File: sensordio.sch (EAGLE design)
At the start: 15 parts

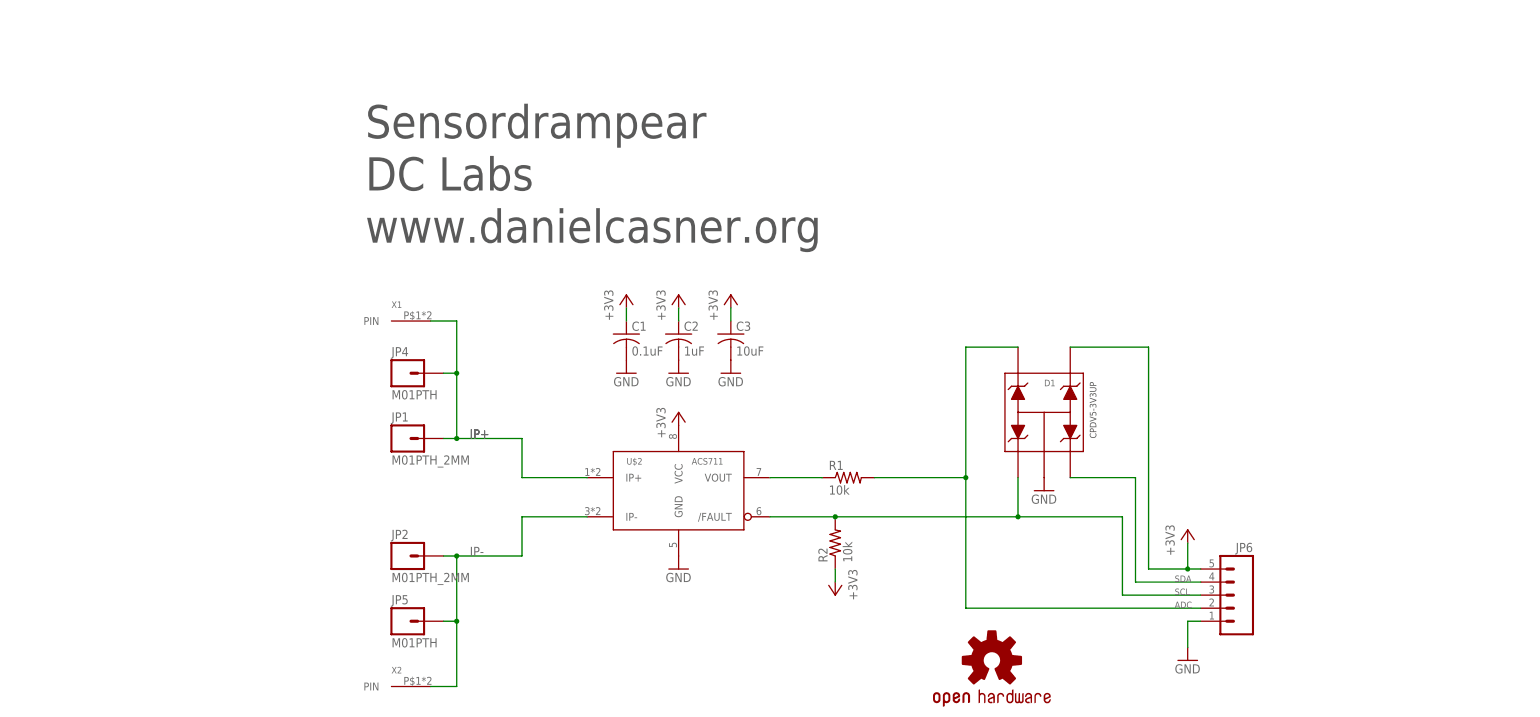
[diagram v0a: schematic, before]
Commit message: Add GPIO extension for sensordrone.
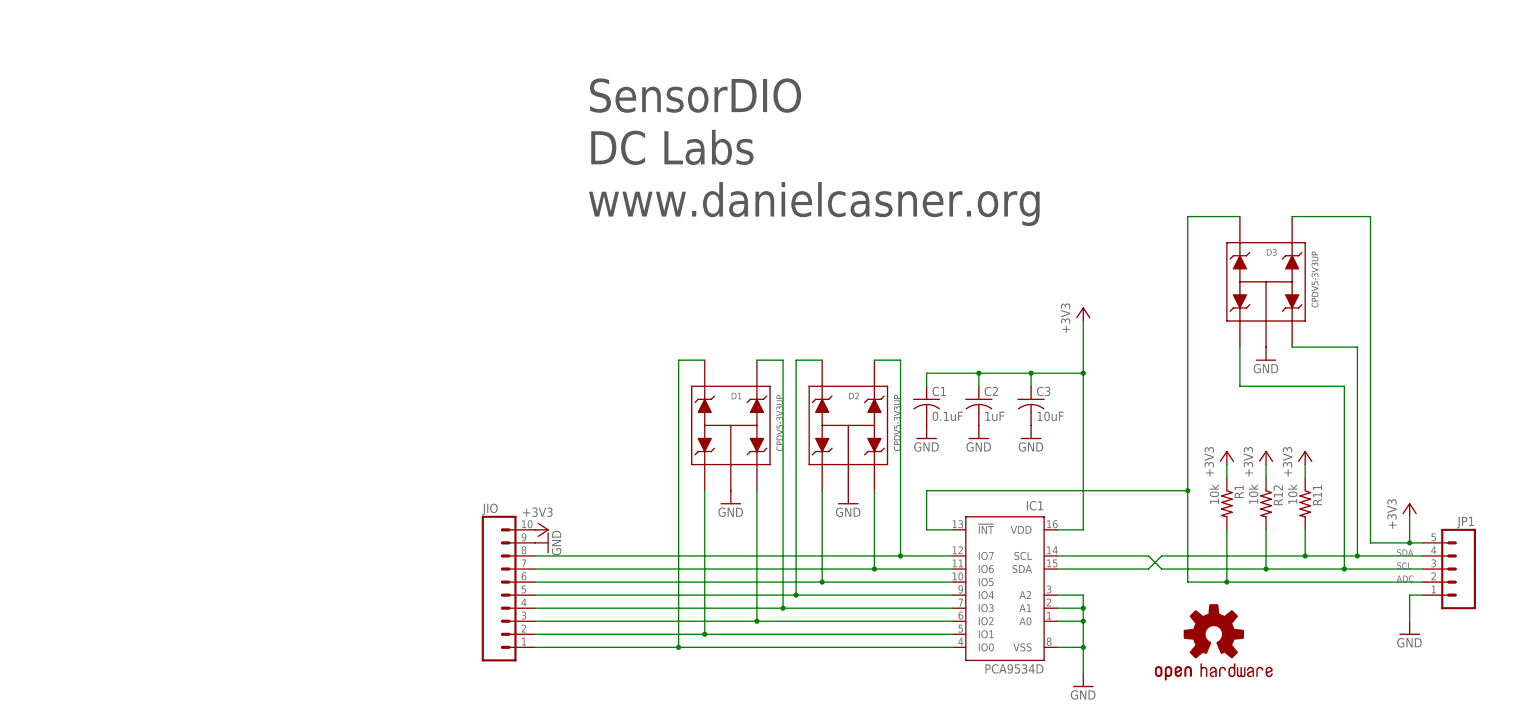
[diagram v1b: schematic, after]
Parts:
- removed JP2: M01PTH_2MM, SparkFun:M01PTH_2MM
- removed JP4, JP5: M01PTH, SparkFun:M01PTH
- removed JP6: (no value), SparkFun-Connectors:M05PTH_LONGPADS
- removed R2: 10k, rcl:R-US_R0402
- removed U$2: ACS711, DMM:ACS711
- removed X1, X2: (no value), DMM:606X
- added D2, D3: CPDV5-3V3UP, DMM:CPDV5
- added IC1: PCA9534D, micro-philips:PCA9534D
- added JIO: (no value), con-amp-quick:M10
- added R11, R12: 10k, rcl:R-US_R0402
- JP1: value M01PTH_2MM -> (none); device SparkFun:M01PTH_2MM -> SparkFun-Connectors:M05PTH_LONGPADS
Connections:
- removed net IP+: JP1.1, JP4.1, U$2.IP+, X1.PIN
- removed net IP-: JP2.1, JP5.1, U$2.IP-, X2.PIN
- new net N$2: D1.P$5, IC1.IO0, JIO.1
- new net N$4: D1.P$3, IC1.IO2, JIO.3
- new net N$5: D1.P$4, IC1.IO3, JIO.4
- new net N$6: D2.P$5, IC1.IO4, JIO.5
- new net N$7: D2.P$1, IC1.IO5, JIO.6
- new net N$8: D2.P$3, IC1.IO6, JIO.7
- new net N$9: D2.P$4, IC1.IO7, JIO.8
- net +3V3: now also D3.P$4, IC1.VDD, JIO.10, JP1.5, R1.1, R11.1, R12.1; no longer D1.P$4, JP6.5, R2.1, U$2.VCC
- net ADC: now also D3.P$5, IC1.!INT, JP1.2; no longer D1.P$5, JP6.2
- net GND: now also D2.P$2, D3.P$2, IC1.A0, IC1.A1, IC1.A2, IC1.VSS, JIO.9, JP1.1; no longer JP6.1, U$2.GND
- net N$3: now also D1.P$1, IC1.IO1, JIO.2; no longer R1.1, U$2.VOUT
- net SCL: now also D3.P$1, IC1.SCL, JP1.3, R12.2; no longer D1.P$1, JP6.3, R2.2, U$2./FAULT
- net SDA: now also D3.P$3, IC1.SDA, JP1.4, R11.2; no longer D1.P$3, JP6.4
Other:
- note added: "SensorDIO"
- note removed: "Sensordrampear"
- moved on the sheet: C1, C2, C3, D1, R1

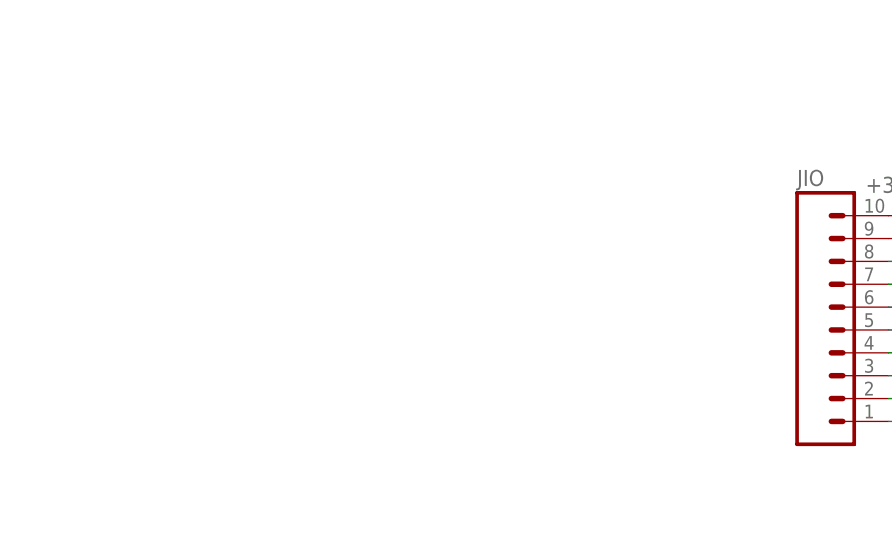
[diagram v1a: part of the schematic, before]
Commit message: Add add-on add-on for SensordrIO
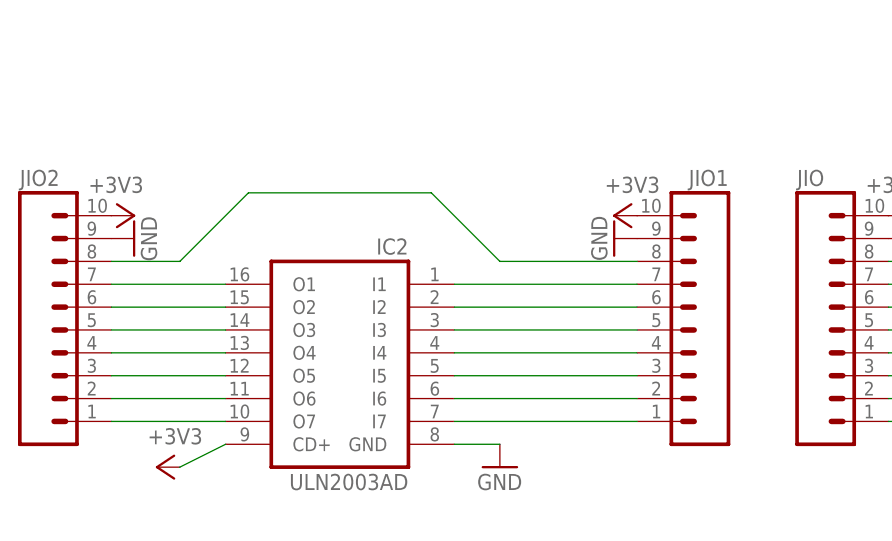
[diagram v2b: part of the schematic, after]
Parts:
- added IC2: ULN2003AD, uln-udn:ULN2003AD
- added JIO1, JIO2: (no value), con-amp-quick:M10
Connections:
- new net N$1: IC2.I7, JIO1.1
- new net N$10: IC2.I6, JIO1.2
- new net N$11: IC2.I5, JIO1.3
- new net N$12: IC2.I4, JIO1.4
- new net N$13: IC2.I3, JIO1.5
- new net N$14: IC2.I2, JIO1.6
- new net N$15: IC2.I1, JIO1.7
- new net N$16: IC2.O7, JIO2.1
- new net N$17: IC2.O6, JIO2.2
- new net N$18: IC2.O5, JIO2.3
- new net N$19: IC2.O4, JIO2.4
- new net N$20: IC2.O3, JIO2.5
- new net N$21: IC2.O2, JIO2.6
- new net N$22: IC2.O1, JIO2.7
- new net N$23: JIO1.8, JIO2.8
- net +3V3: now also IC2.CD+, JIO1.10, JIO2.10
- net GND: now also IC2.GND, JIO1.9, JIO2.9
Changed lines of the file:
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@@
 <part name="GND8" library="supply1" deviceset="GND" device=""/>
 <part name="+3V6" library="supply1" deviceset="+3V3" device=""/>
+<part name="IC2" library="uln-udn" deviceset="ULN2003A" device="D"/>
+<part name="JIO1" library="con-amp-quick" deviceset="M10" device=""/>
+<part name="JIO2" library="con-amp-quick" deviceset="M10" device=""/>
+<part name="GND9" library="supply1" deviceset="GND" device=""/>
+<part name="GND10" library="supply1" deviceset="GND" device=""/>
+<part name="GND12" library="supply1" deviceset="GND" device=""/>
+<part name="+3V7" library="supply1" deviceset="+3V3" device=""/>
+<part name="+3V8" library="supply1" deviceset="+3V3" device=""/>
+<part name="+3V9" library="supply1" deviceset="+3V3" device=""/>
 </parts>
 <sheets>
@@
 <instance part="GND8" gate="1" x="-86.36" y="22.86" rot="R90"/>
 <instance part="+3V6" gate="G$1" x="-86.36" y="25.4" rot="R270"/>
+<instance part="IC2" gate="A" x="-149.86" y="10.16" rot="MR0"/>
+<instance part="JIO1" gate="G$1" x="-111.76" y="15.24" rot="MR0"/>
+<instance part="JIO2" gate="G$1" x="-180.34" y="15.24"/>
+<instance part="GND9" gate="1" x="-132.08" y="-2.54"/>
+<instance part="GND10" gate="1" x="-119.38" y="22.86" rot="R270"/>
+<instance part="GND12" gate="1" x="-172.72" y="22.86" rot="R90"/>
+<instance part="+3V7" gate="G$1" x="-172.72" y="25.4" rot="R270"/>
+<instance part="+3V8" gate="G$1" x="-119.38" y="25.4" rot="MR270"/>
+<instance part="+3V9" gate="G$1" x="-170.18" y="-2.54" rot="MR270"/>
 </instances>
 <busses>
@@
 <pinref part="JIO" gate="G$1" pin="9"/>
 <pinref part="GND8" gate="1" pin="GND"/>
+</segment>
+<segment>
+<pinref part="IC2" gate="A" pin="GND"/>
+<pinref part="GND9" gate="1" pin="GND"/>
+<wire x1="-132.08" y1="0" x2="-137.16" y2="0" width="0.1524" layer="91"/>
+</segment>
+<segment>
+<pinref part="JIO1" gate="G$1" pin="9"/>
+<pinref part="GND10" gate="1" pin="GND"/>
+</segment>
+<segment>
+<pinref part="JIO2" gate="G$1" pin="9"/>
+<pinref part="GND12" gate="1" pin="GND"/>
 </segment>
 </net>
@@
 <pinref part="+3V6" gate="G$1" pin="+3V3"/>
 </segment>
+<segment>
+<pinref part="JIO2" gate="G$1" pin="10"/>
+<pinref part="+3V7" gate="G$1" pin="+3V3"/>
+</segment>
+<segment>
+<pinref part="JIO1" gate="G$1" pin="10"/>
+<pinref part="+3V8" gate="G$1" pin="+3V3"/>
+</segment>
+<segment>
+<pinref part="IC2" gate="A" pin="CD+"/>
+<pinref part="+3V9" gate="G$1" pin="+3V3"/>
+<wire x1="-167.64" y1="-2.54" x2="-162.56" y2="0" width="0.1524" layer="91"/>
+</segment>
 </net>
 <net name="SDA" class="0">
@@
 </segment>
 </net>
+<net name="N$1" class="0">
+<segment>
+<pinref part="JIO1" gate="G$1" pin="1"/>
+<pinref part="IC2" gate="A" pin="I7"/>
+<wire x1="-116.84" y1="2.54" x2="-137.16" y2="2.54" width="0.1524" layer="91"/>
+</segment>
+</net>
+<net name="N$10" class="0">
+<segment>
+<pinref part="JIO1" gate="G$1" pin="2"/>
+<pinref part="IC2" gate="A" pin="I6"/>
+<wire x1="-116.84" y1="5.08" x2="-137.16" y2="5.08" width="0.1524" layer="91"/>
+</segment>
+</net>
+<net name="N$11" class="0">
+<segment>
+<pinref part="JIO1" gate="G$1" pin="3"/>
+<pinref part="IC2" gate="A" pin="I5"/>
+<wire x1="-116.84" y1="7.62" x2="-137.16" y2="7.62" width="0.1524" layer="91"/>
+</segment>
+</net>
+<net name="N$12" class="0">
+<segment>
+<pinref part="JIO1" gate="G$1" pin="4"/>
+<pinref part="IC2" gate="A" pin="I4"/>
+<wire x1="-116.84" y1="10.16" x2="-137.16" y2="10.16" width="0.1524" layer="91"/>
+</segment>
+</net>
+<net name="N$13" class="0">
+<segment>
+<pinref part="JIO1" gate="G$1" pin="5"/>
+<pinref part="IC2" gate="A" pin="I3"/>
+<wire x1="-116.84" y1="12.7" x2="-137.16" y2="12.7" width="0.1524" layer="91"/>
+</segment>
+</net>
+<net name="N$14" class="0">
+<segment>
+<pinref part="JIO1" gate="G$1" pin="6"/>
+<pinref part="IC2" gate="A" pin="I2"/>
+<wire x1="-116.84" y1="15.24" x2="-137.16" y2="15.24" width="0.1524" layer="91"/>
+</segment>
+</net>
+<net name="N$15" class="0">
+<segment>
+<pinref part="JIO1" gate="G$1" pin="7"/>
+<pinref part="IC2" gate="A" pin="I1"/>
+<wire x1="-116.84" y1="17.78" x2="-137.16" y2="17.78" width="0.1524" layer="91"/>
+</segment>
+</net>
+<net name="N$16" class="0">
+<segment>
+<pinref part="JIO2" gate="G$1" pin="1"/>
+<pinref part="IC2" gate="A" pin="O7"/>
+<wire x1="-175.26" y1="2.54" x2="-162.56" y2="2.54" width="0.1524" layer="91"/>
+</segment>
+</net>
+<net name="N$17" class="0">
+<segment>
+<pinref part="JIO2" gate="G$1" pin="2"/>
+<pinref part="IC2" gate="A" pin="O6"/>
+<wire x1="-175.26" y1="5.08" x2="-162.56" y2="5.08" width="0.1524" layer="91"/>
+</segment>
+</net>
+<net name="N$18" class="0">
+<segment>
+<pinref part="JIO2" gate="G$1" pin="3"/>
+<pinref part="IC2" gate="A" pin="O5"/>
+<wire x1="-175.26" y1="7.62" x2="-162.56" y2="7.62" width="0.1524" layer="91"/>
+</segment>
+</net>
+<net name="N$19" class="0">
+<segment>
+<pinref part="JIO2" gate="G$1" pin="4"/>
+<pinref part="IC2" gate="A" pin="O4"/>
+<wire x1="-175.26" y1="10.16" x2="-162.56" y2="10.16" width="0.1524" layer="91"/>
+</segment>
+</net>
+<net name="N$20" class="0">
+<segment>
+<pinref part="JIO2" gate="G$1" pin="5"/>
+<pinref part="IC2" gate="A" pin="O3"/>
+<wire x1="-175.26" y1="12.7" x2="-162.56" y2="12.7" width="0.1524" layer="91"/>
+</segment>
+</net>
+<net name="N$21" class="0">
+<segment>
+<pinref part="JIO2" gate="G$1" pin="6"/>
+<pinref part="IC2" gate="A" pin="O2"/>
+<wire x1="-175.26" y1="15.24" x2="-162.56" y2="15.24" width="0.1524" layer="91"/>
+</segment>
+</net>
+<net name="N$22" class="0">
+<segment>
+<pinref part="JIO2" gate="G$1" pin="7"/>
+<pinref part="IC2" gate="A" pin="O1"/>
+<wire x1="-175.26" y1="17.78" x2="-162.56" y2="17.78" width="0.1524" layer="91"/>
+</segment>
+</net>
+<net name="N$23" class="0">
+<segment>
+<pinref part="JIO2" gate="G$1" pin="8"/>
+<wire x1="-175.26" y1="20.32" x2="-167.64" y2="20.32" width="0.1524" layer="91"/>
+<wire x1="-167.64" y1="20.32" x2="-160.02" y2="27.94" width="0.1524" layer="91"/>
+<wire x1="-160.02" y1="27.94" x2="-139.7" y2="27.94" width="0.1524" layer="91"/>
+<wire x1="-139.7" y1="27.94" x2="-132.08" y2="20.32" width="0.1524" layer="91"/>
+<pinref part="JIO1" gate="G$1" pin="8"/>
+<wire x1="-132.08" y1="20.32" x2="-116.84" y2="20.32" width="0.1524" layer="91"/>
+</segment>
+</net>

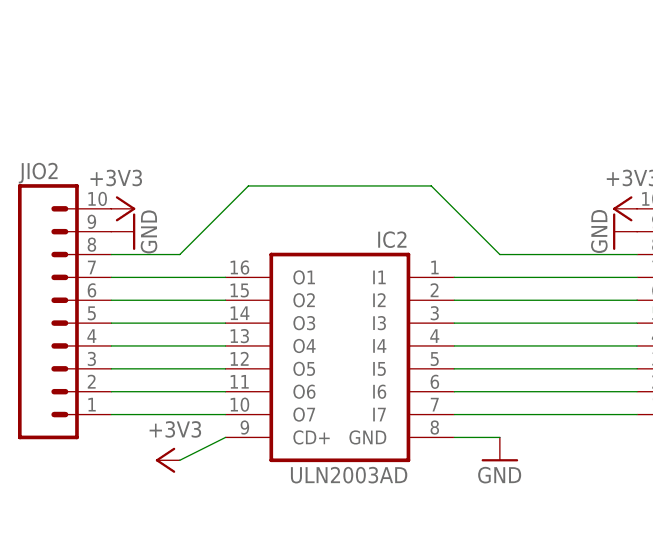
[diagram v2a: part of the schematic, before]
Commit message: Add pin signal labels
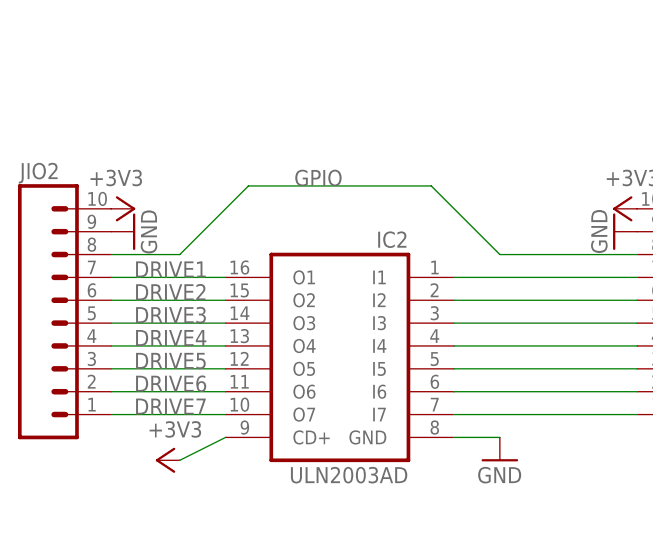
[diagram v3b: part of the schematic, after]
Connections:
- net N$16 renamed DRIVE7
- net N$17 renamed DRIVE6
- net N$18 renamed DRIVE5
- net N$19 renamed DRIVE4
- net N$20 renamed DRIVE3
- net N$21 renamed DRIVE2
- net N$22 renamed DRIVE1
- net N$23 renamed GPIO
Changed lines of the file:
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@@
 </segment>
 </net>
-<net name="N$16" class="0">
+<net name="DRIVE7" class="0">
 <segment>
 <pinref part="JIO2" gate="G$1" pin="1"/>
 <pinref part="IC2" gate="A" pin="O7"/>
 <wire x1="-175.26" y1="2.54" x2="-162.56" y2="2.54" width="0.1524" layer="91"/>
+<label x="-172.72" y="2.54" size="1.778" layer="95"/>
 </segment>
 </net>
-<net name="N$17" class="0">
+<net name="DRIVE6" class="0">
 <segment>
 <pinref part="JIO2" gate="G$1" pin="2"/>
 <pinref part="IC2" gate="A" pin="O6"/>
 <wire x1="-175.26" y1="5.08" x2="-162.56" y2="5.08" width="0.1524" layer="91"/>
+<label x="-172.72" y="5.08" size="1.778" layer="95"/>
 </segment>
 </net>
-<net name="N$18" class="0">
+<net name="DRIVE5" class="0">
 <segment>
 <pinref part="JIO2" gate="G$1" pin="3"/>
 <pinref part="IC2" gate="A" pin="O5"/>
 <wire x1="-175.26" y1="7.62" x2="-162.56" y2="7.62" width="0.1524" layer="91"/>
+<label x="-172.72" y="7.62" size="1.778" layer="95"/>
 </segment>
 </net>
-<net name="N$19" class="0">
+<net name="DRIVE4" class="0">
 <segment>
 <pinref part="JIO2" gate="G$1" pin="4"/>
 <pinref part="IC2" gate="A" pin="O4"/>
 <wire x1="-175.26" y1="10.16" x2="-162.56" y2="10.16" width="0.1524" layer="91"/>
+<label x="-172.72" y="10.16" size="1.778" layer="95"/>
 </segment>
 </net>
-<net name="N$20" class="0">
+<net name="DRIVE3" class="0">
 <segment>
 <pinref part="JIO2" gate="G$1" pin="5"/>
 <pinref part="IC2" gate="A" pin="O3"/>
 <wire x1="-175.26" y1="12.7" x2="-162.56" y2="12.7" width="0.1524" layer="91"/>
+<label x="-172.72" y="12.7" size="1.778" layer="95"/>
 </segment>
 </net>
-<net name="N$21" class="0">
+<net name="DRIVE2" class="0">
 <segment>
 <pinref part="JIO2" gate="G$1" pin="6"/>
 <pinref part="IC2" gate="A" pin="O2"/>
 <wire x1="-175.26" y1="15.24" x2="-162.56" y2="15.24" width="0.1524" layer="91"/>
+<label x="-172.72" y="15.24" size="1.778" layer="95"/>
 </segment>
 </net>
-<net name="N$22" class="0">
+<net name="DRIVE1" class="0">
 <segment>
 <pinref part="JIO2" gate="G$1" pin="7"/>
 <pinref part="IC2" gate="A" pin="O1"/>
 <wire x1="-175.26" y1="17.78" x2="-162.56" y2="17.78" width="0.1524" layer="91"/>
+<label x="-172.72" y="17.78" size="1.778" layer="95"/>
 </segment>
 </net>
-<net name="N$23" class="0">
+<net name="GPIO" class="0">
 <segment>
 <pinref part="JIO2" gate="G$1" pin="8"/>
@@
 <pinref part="JIO1" gate="G$1" pin="8"/>
 <wire x1="-132.08" y1="20.32" x2="-116.84" y2="20.32" width="0.1524" layer="91"/>
+<label x="-154.94" y="27.94" size="1.778" layer="95"/>
 </segment>
 </net>
